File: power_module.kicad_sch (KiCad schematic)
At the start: 3 parts, among them J2 OUTPUT, J3 I2C_BREAKOUT, SW1 ON_OFF

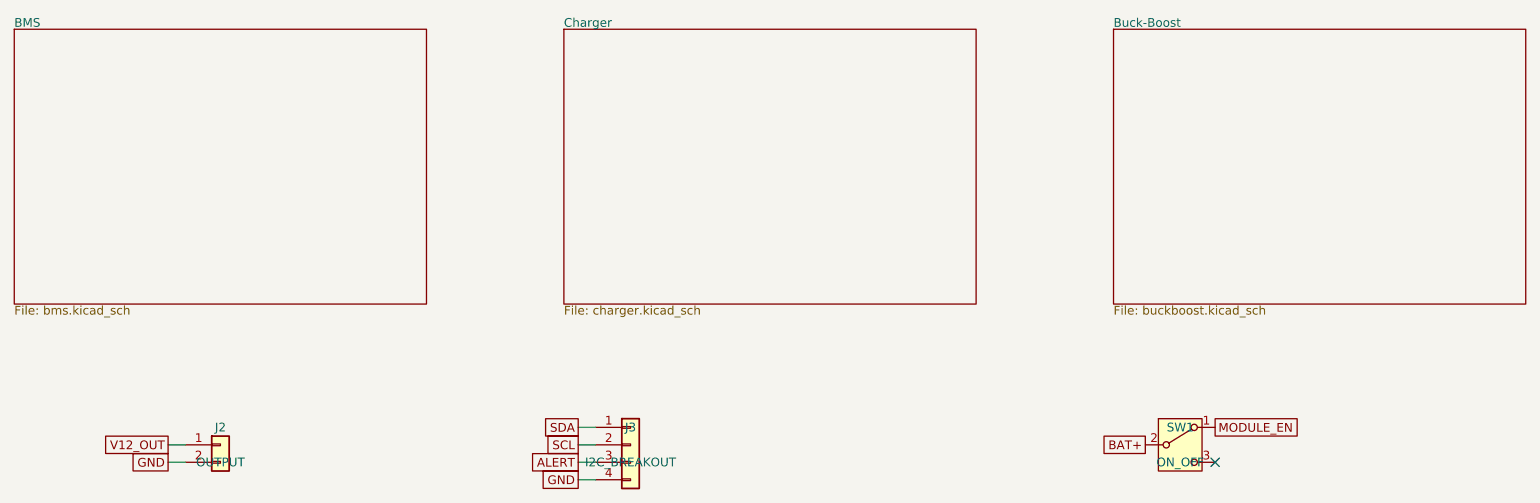
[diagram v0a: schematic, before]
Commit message: Moved U4 to bottom, away from pads and away from cells.  Swapped SMD thermistor for THT and moved to B.Cu.  Locked thermistor and BAT1.
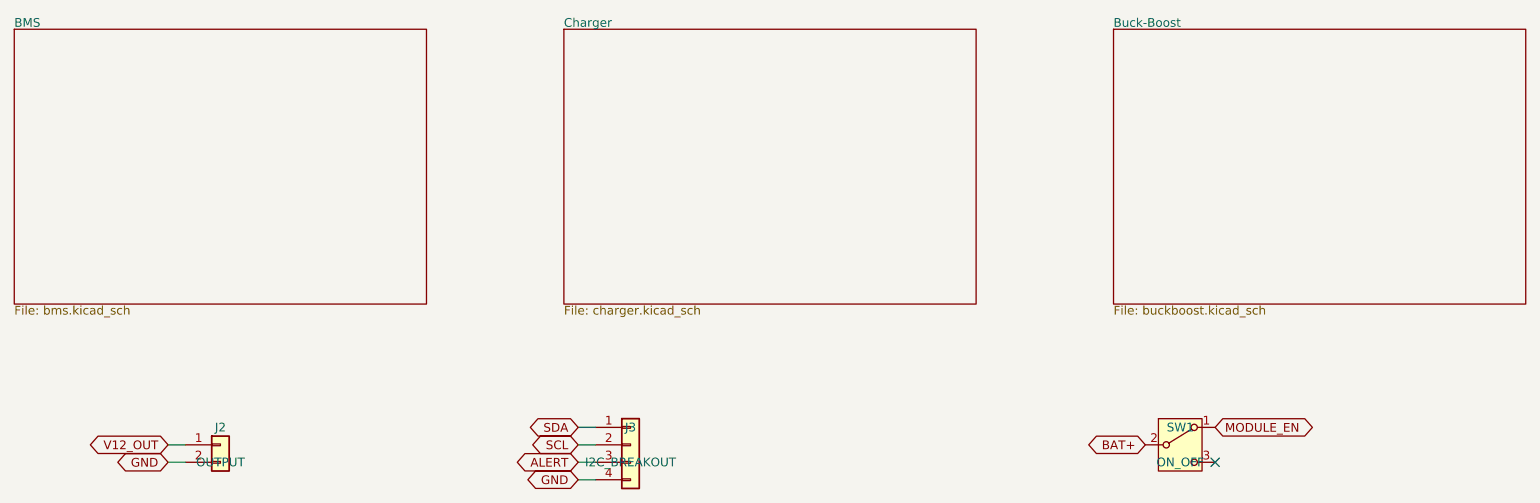
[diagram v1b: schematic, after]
